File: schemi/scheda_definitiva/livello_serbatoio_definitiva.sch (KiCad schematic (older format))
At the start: 35 parts, among them J1 USB_B, J2 CONN_US, J3 CONN_LCD, SW1 SW_RST, SW2 SW_LCDON, U1 FT232RL, U2 ATmega328P-PU, Y1 16MHz

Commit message: fix a schema definitivo e assegnate footprint
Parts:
- removed D5: LED_LL, symbol Device:LED
- removed SW2: SW_LCDON, symbol Switch:SW_Push
- added J4: BTN_LED_GROUP, Connector_Molex:Molex_Micro-Latch_53254-0470_1x04_P2.00mm_Horizontal, symbol Connector:Conn_01x04_Male
- C1, C2, C3, C4, C5, C6, C7, C8: footprint (none) -> Capacitor_THT:C_Axial_L3.8mm_D2.6mm_P7.50mm_Horizontal
- D1, D2, D4: footprint (none) -> LED_THT:LED_D3.0mm
- D3: footprint (none) -> Diode_THT:D_DO-35_SOD27_P7.62mm_Horizontal
- F1: footprint (none) -> Fuse:Fuse_Littelfuse-LVR100
- J1: footprint (none) -> Connector_USB:USB_B_OST_USB-B1HSxx_Horizontal
- J2: footprint (none) -> Connector_PinHeader_1.00mm:PinHeader_1x04_P1.00mm_Vertical
- J3: footprint (none) -> Connector_PinHeader_1.00mm:PinHeader_1x16_P1.00mm_Vertical
- L1: footprint (none) -> Inductor_THT:L_Axial_L6.6mm_D2.7mm_P10.16mm_Horizontal_Vishay_IM-2
- R1, R2: value 22R -> 1k; footprint (none) -> Resistor_THT:R_Axial_DIN0207_L6.3mm_D2.5mm_P7.62mm_Horizontal
- R10, R11, R3, R4, R5, R6, R7, R8, R9: footprint (none) -> Resistor_THT:R_Axial_DIN0207_L6.3mm_D2.5mm_P7.62mm_Horizontal
- RV1: footprint (none) -> Potentiometer_THT:Potentiometer_Vishay_T73YP_Vertical
- SW1: footprint (none) -> Button_Switch_THT:SW_PUSH_6mm
- Y1: footprint (none) -> simboli_custom:Crystal_TH_AS16_5mm
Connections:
- net labels added: RX, TX
- wire segments 159 -> 154
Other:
- moved on the sheet: D4, J3, R10, R11, R8, R9, RV1

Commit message: caricamento prima bozza PCB + piccoli fix a footprint
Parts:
- J2: footprint Connector_PinHeader_1.00mm:PinHeader_1x04_P1.00mm_Vertical -> Connector_Molex:Molex_Micro-Latch_53254-0470_1x04_P2.00mm_Horizontal
- J3: footprint Connector_PinHeader_1.00mm:PinHeader_1x16_P1.00mm_Vertical -> Connector_PinHeader_1.27mm:PinHeader_1x16_P1.27mm_Vertical
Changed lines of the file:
@@
 F 0 "J2" H 10500 1050 50  0000 C CNN
 F 1 "CONN_US" H 10750 1300 50  0000 C CNN
-F 2 "Connector_PinHeader_1.00mm:PinHeader_1x04_P1.00mm_Vertical" H 10500 1350 50  0001 C CNN
+F 2 "Connector_Molex:Molex_Micro-Latch_53254-0470_1x04_P2.00mm_Horizontal" H 10500 1350 50  0001 C CNN
 F 3 "~" H 10500 1350 50  0001 C CNN
 	1    10500 1350
@@
 F 0 "J3" H 10492 3125 50  0000 C CNN
 F 1 "CONN_LCD" H 10492 3216 50  0000 C CNN
-F 2 "Connector_PinHeader_1.00mm:PinHeader_1x16_P1.00mm_Vertical" H 10600 4150 50  0001 C CNN
+F 2 "Connector_PinHeader_1.27mm:PinHeader_1x16_P1.27mm_Vertical" H 10600 4150 50  0001 C CNN
 F 3 "~" H 10600 4150 50  0001 C CNN
 	1    10600 4150

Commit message: modifiche a scheda definitiva - aggiunto footprint LCD di riferimento - modificato schematico per aggiungere connettore ICSP e fori di montaggio a massa - ricollocati connettori - da rivedere collocazione MCU per conflitto con LCD
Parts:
- removed R10: 390, Resistor_THT:R_Axial_DIN0207_L6.3mm_D2.5mm_P7.62mm_Horizontal, symbol Device:R
- added H1: HOLE1, MountingHole:MountingHole_3mm_Pad_Via, symbol Mechanical:MountingHole_Pad
- added H2: HOLE2, MountingHole:MountingHole_3mm_Pad_Via, symbol Mechanical:MountingHole_Pad
- added H3: HOLE3, MountingHole:MountingHole_3mm_Pad_Via, symbol Mechanical:MountingHole_Pad
- added H4: HOLE4, MountingHole:MountingHole_3mm_Pad_Via, symbol Mechanical:MountingHole_Pad
- added J5: Conn_01x06_Male, Connector_PinHeader_2.54mm:PinHeader_1x06_P2.54mm_Horizontal, symbol Connector:Conn_01x06_Male
- J3: footprint Connector_PinHeader_1.27mm:PinHeader_1x16_P1.27mm_Vertical -> Connector_PinSocket_2.54mm:PinSocket_1x16_P2.54mm_Vertical
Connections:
- net labels added: ICSP_MISO, ICSP_MOSI, ICSP_RST, ICSP_SCK
- wire segments 154 -> 179
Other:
- note added: "ICSP - Bootloader"
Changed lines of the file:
@@
 Text GLabel 6800 2450 2    50   Output ~ 0
 D11
-Wire Wire Line
-	6650 2450 6800 2450
-Wire Wire Line
-	6650 2550 6800 2550
 Text GLabel 6800 2550 2    50   Input ~ 0
 D12
@@
 D13
 Wire Wire Line
-	6650 2650 6800 2650
+	6650 2650 6750 2650
 $Comp
 L power:GND #PWR06
@@
 Wire Notes Line
 	10850 2600 10850 6300
-Text GLabel 9500 4400 2    50   Output ~ 0
+Text GLabel 9100 4400 2    50   Output ~ 0
 BLA
-$Comp
-L Device:R R10
-U 1 1 5F131632
-P 9150 4400
-F 0 "R10" V 9050 4400 50  0000 C CNN
-F 1 "390" V 9150 4400 50  0000 C CNN
-F 2 "Resistor_THT:R_Axial_DIN0207_L6.3mm_D2.5mm_P7.62mm_Horizontal" V 9080 4400 50  0001 C CNN
-F 3 "~" H 9150 4400 50  0001 C CNN
-	1    9150 4400
-	0    1    1    0
-$EndComp
-Text GLabel 8800 4400 0    50   Input ~ 0
+Text GLabel 8850 4400 0    50   Input ~ 0
 D9
-Wire Wire Line
-	8800 4400 9000 4400
-Wire Wire Line
-	9300 4400 9500 4400
 $Comp
 L power:VCC #PWR018
@@
 F 0 "J3" H 10492 3125 50  0000 C CNN
 F 1 "CONN_LCD" H 10492 3216 50  0000 C CNN
-F 2 "Connector_PinHeader_1.27mm:PinHeader_1x16_P1.27mm_Vertical" H 10600 4150 50  0001 C CNN
+F 2 "Connector_PinSocket_2.54mm:PinSocket_1x16_P2.54mm_Vertical" H 10600 4150 50  0001 C CNN
 F 3 "~" H 10600 4150 50  0001 C CNN
 	1    10600 4150
@@
 Wire Wire Line
 	8100 1600 8100 1850
+Wire Wire Line
+	8850 4400 9100 4400
+Wire Notes Line
+	5400 5350 8050 5350
+Wire Notes Line
+	8050 5350 8050 6450
+Wire Notes Line
+	8050 6450 5400 6450
+Wire Notes Line
+	5400 6450 5400 5350
+Text Notes 6350 5450 0    50   ~ 0
+ICSP - Bootloader
+$Comp
+L Connector:Conn_01x06_Male J5
+U 1 1 5F49926C
+P 7150 5900
+F 0 "J5" H 7122 5782 50  0000 R CNN
+F 1 "Conn_01x06_Male" H 7550 6200 50  0000 R CNN
+F 2 "Connector_PinHeader_2.54mm:PinHeader_1x06_P2.54mm_Horizontal" H 7150 5900 50  0001 C CNN
+F 3 "~" H 7150 5900 50  0001 C CNN
+	1    7150 5900
+	-1   0    0    1
+$EndComp
+Text GLabel 6550 6100 0    50   Input ~ 0
+ICSP_MISO
+Text GLabel 6550 5800 0    50   Input ~ 0
+ICSP_MOSI
+$Comp
+L power:VCC #PWR017
+U 1 1 5F4B97E7
+P 6550 6000
+F 0 "#PWR017" H 6550 5850 50  0001 C CNN
+F 1 "VCC" V 6565 6127 50  0000 L CNN
+F 2 "" H 6550 6000 50  0001 C CNN
+F 3 "" H 6550 6000 50  0001 C CNN
+	1    6550 6000
+	0    -1   -1   0
+$EndComp
+Text GLabel 6550 5900 0    50   Input ~ 0
+ICSP_SCK
+Text GLabel 6550 5700 0    50   Input ~ 0
+ICSP_RST
+$Comp
+L power:GND #PWR07
+U 1 1 5F4BAD5C
+P 6550 5600
+F 0 "#PWR07" H 6550 5350 50  0001 C CNN
+F 1 "GND" V 6555 5472 50  0000 R CNN
+F 2 "" H 6550 5600 50  0001 C CNN
+F 3 "" H 6550 5600 50  0001 C CNN
+	1    6550 5600
+	0    1    1    0
+$EndComp
+Wire Wire Line
+	6550 5600 6950 5600
+Wire Wire Line
+	6550 5700 6950 5700
+Wire Wire Line
+	6550 5800 6950 5800
+Wire Wire Line
+	6550 5900 6950 5900
+Wire Wire Line
+	6550 6000 6950 6000
+Wire Wire Line
+	6550 6100 6950 6100
+Text GLabel 7100 2350 2    50   Output ~ 0
+ICSP_MISO
+Text GLabel 7100 2250 2    50   Output ~ 0
+ICSP_MOSI
+Text GLabel 7100 2450 2    50   Output ~ 0
+ICSP_SCK
+Wire Wire Line
+	7000 2450 7000 2700
+Wire Wire Line
+	7000 2700 6750 2700
+Wire Wire Line
+	6750 2700 6750 2650
+Wire Wire Line
+	7000 2450 7100 2450
+Connection ~ 6750 2650
+Wire Wire Line
+	6750 2650 6800 2650
+Wire Wire Line
+	6650 2450 6700 2450
+Wire Wire Line
+	6650 2550 6750 2550
+Wire Wire Line
+	7100 2350 6750 2350
+Wire Wire Line
+	6750 2350 6750 2550
+Connection ~ 6750 2550
+Wire Wire Line
+	6750 2550 6800 2550
+Wire Wire Line
+	7100 2250 7050 2250
+Wire Wire Line
+	7050 2250 7050 2300
+Wire Wire Line
+	7050 2300 6700 2300
+Wire Wire Line
+	6700 2300 6700 2450
+Connection ~ 6700 2450
+Wire Wire Line
+	6700 2450 6800 2450
+Text GLabel 3600 5950 3    50   Output ~ 0
+ICSP_RST
+Wire Wire Line
+	3600 5700 3600 5950
+$Comp
+L Mechanical:MountingHole_Pad H1
+U 1 1 5F5C5141
+P 2500 1000
+F 0 "H1" H 2600 1049 50  0000 L CNN
+F 1 "HOLE1" H 2400 1200 50  0000 L CNN
+F 2 "MountingHole:MountingHole_3mm_Pad_Via" H 2500 1000 50  0001 C CNN
+F 3 "~" H 2500 1000 50  0001 C CNN
+	1    2500 1000
+	1    0    0    -1
+$EndComp
+$Comp
+L Mechanical:MountingHole_Pad H2
+U 1 1 5F5C614B
+P 2850 1000
+F 0 "H2" H 2950 1049 50  0000 L CNN
+F 1 "HOLE2" H 2800 1200 50  0000 L CNN
+F 2 "MountingHole:MountingHole_3mm_Pad_Via" H 2850 1000 50  0001 C CNN
+F 3 "~" H 2850 1000 50  0001 C CNN
+	1    2850 1000
+	1    0    0    -1
+$EndComp
+$Comp
+L Mechanical:MountingHole_Pad H3
+U 1 1 5F5C6841
+P 3200 1000
+F 0 "H3" H 3300 1049 50  0000 L CNN
+F 1 "HOLE3" H 3100 1200 50  0000 L CNN
+F 2 "MountingHole:MountingHole_3mm_Pad_Via" H 3200 1000 50  0001 C CNN
+F 3 "~" H 3200 1000 50  0001 C CNN
+	1    3200 1000
+	1    0    0    -1
+$EndComp
+$Comp
+L Mechanical:MountingHole_Pad H4
+U 1 1 5F5C77FA
+P 3550 1000
+F 0 "H4" H 3650 1049 50  0000 L CNN
+F 1 "HOLE4" H 3450 1200 50  0000 L CNN
+F 2 "MountingHole:MountingHole_3mm_Pad_Via" H 3550 1000 50  0001 C CNN
+F 3 "~" H 3550 1000 50  0001 C CNN
+	1    3550 1000
+	1    0    0    -1
+$EndComp
+$Comp
+L power:GND #PWR022
+U 1 1 5F5C8BD6
+P 3050 1300
+F 0 "#PWR022" H 3050 1050 50  0001 C CNN
+F 1 "GND" H 3055 1127 50  0000 C CNN
+F 2 "" H 3050 1300 50  0001 C CNN
+F 3 "" H 3050 1300 50  0001 C CNN
+	1    3050 1300
+	1    0    0    -1
+$EndComp
+Wire Wire Line
+	2500 1100 2850 1100
+Wire Wire Line
+	2850 1100 3200 1100
+Connection ~ 2850 1100
+Wire Wire Line
+	3200 1100 3550 1100
+Connection ~ 3200 1100
+Wire Wire Line
+	3200 1100 3200 1150
+Wire Wire Line
+	3200 1150 3050 1150
+Wire Wire Line
+	3050 1150 3050 1300
 $EndSCHEMATC

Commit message: riposizionati connettori + auto-routing eseguito con freerouting
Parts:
- removed C5: 100nF, Capacitor_THT:C_Axial_L3.8mm_D2.6mm_P7.50mm_Horizontal, symbol Device:C
- removed L1: 10uH, Inductor_THT:L_Axial_L6.6mm_D2.7mm_P10.16mm_Horizontal_Vishay_IM-2, symbol Device:L
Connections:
- wire segments 179 -> 173
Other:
- moved on the sheet: C6
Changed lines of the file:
@@
 $EndDescr
-$Comp
-L MCU_Microchip_ATmega:ATmega328P-PU U2
-U 1 1 5F0B08F0
-P 6050 3350
-F 0 "U2" H 5650 4800 50  0000 R CNN
-F 1 "ATmega328P-PU" H 6250 3600 50  0000 R CNN
-F 2 "Package_DIP:DIP-28_W7.62mm" H 6050 3350 50  0001 C CIN
-F 3 "http://ww1.microchip.com/downloads/en/DeviceDoc/ATmega328_P%20AVR%20MCU%20with%20picoPower%20Technology%20Data%20Sheet%2040001984A.pdf" H 6050 3350 50  0001 C CNN
-	1    6050 3350
-	1    0    0    -1
-$EndComp
 $Comp
 L Interface_USB:FT232RL U1
@@
 Connection ~ 7500 2650
 $Comp
-L Device:C C5
-U 1 1 5F1D4DDB
-P 6550 1350
-F 0 "C5" V 6298 1350 50  0000 C CNN
-F 1 "100nF" V 6389 1350 50  0000 C CNN
-F 2 "Capacitor_THT:C_Axial_L3.8mm_D2.6mm_P7.50mm_Horizontal" H 6588 1200 50  0001 C CNN
-F 3 "~" H 6550 1350 50  0001 C CNN
-	1    6550 1350
-	0    1    1    0
-$EndComp
-$Comp
 L power:GND #PWR08
 U 1 1 5F1D54A8
-P 6900 1650
-F 0 "#PWR08" H 6900 1400 50  0001 C CNN
-F 1 "GND" V 6905 1522 50  0000 R CNN
-F 2 "" H 6900 1650 50  0001 C CNN
-F 3 "" H 6900 1650 50  0001 C CNN
-	1    6900 1650
+P 6700 1700
+F 0 "#PWR08" H 6700 1450 50  0001 C CNN
+F 1 "GND" V 6705 1572 50  0000 R CNN
+F 2 "" H 6700 1700 50  0001 C CNN
+F 3 "" H 6700 1700 50  0001 C CNN
+	1    6700 1700
 	0    -1   -1   0
 $EndComp
@@
 L Device:C C6
 U 1 1 5F0BF95B
-P 6550 1750
-F 0 "C6" V 6298 1750 50  0000 C CNN
-F 1 "100nF" V 6389 1750 50  0000 C CNN
-F 2 "Capacitor_THT:C_Axial_L3.8mm_D2.6mm_P7.50mm_Horizontal" H 6588 1600 50  0001 C CNN
-F 3 "~" H 6550 1750 50  0001 C CNN
-	1    6550 1750
-	0    1    1    0
-$EndComp
-$Comp
-L Device:L L1
-U 1 1 5F0F5110
-P 6150 1600
-F 0 "L1" H 6203 1646 50  0000 L CNN
-F 1 "10uH" H 6203 1555 50  0000 L CNN
-F 2 "Inductor_THT:L_Axial_L6.6mm_D2.7mm_P10.16mm_Horizontal_Vishay_IM-2" H 6150 1600 50  0001 C CNN
-F 3 "~" H 6150 1600 50  0001 C CNN
-	1    6150 1600
-	1    0    0    -1
-$EndComp
-Wire Wire Line
-	6400 1350 6050 1350
-Wire Wire Line
-	6150 1450 6150 950
-Wire Wire Line
-	6050 1350 6050 950
-Wire Wire Line
-	6150 1750 6400 1750
-Wire Wire Line
-	6700 1350 6900 1350
-Wire Wire Line
-	6900 1350 6900 1650
-Wire Wire Line
-	6900 1650 6900 1750
-Wire Wire Line
-	6900 1750 6700 1750
-Connection ~ 6900 1650
+P 6450 1700
+F 0 "C6" V 6700 1700 50  0000 C CNN
+F 1 "100nF" V 6600 1700 50  0000 C CNN
+F 2 "Capacitor_THT:C_Axial_L3.8mm_D2.6mm_P7.50mm_Horizontal" H 6488 1550 50  0001 C CNN
+F 3 "~" H 6450 1700 50  0001 C CNN
+	1    6450 1700
+	0    -1   -1   0
+$EndComp
 $Comp
 L power:GND #PWR02
@@
 NoConn ~ 3850 3950
 NoConn ~ 3850 4050
-Wire Wire Line
-	6050 1350 6050 1850
-Connection ~ 6050 1350
 Text GLabel 6800 4050 2    50   Input ~ 0
 D2
@@
 Connection ~ 3150 2350
 Connection ~ 2950 2350
-Wire Wire Line
-	6150 1850 6150 1750
-Connection ~ 6150 1750
 Wire Wire Line
 	2150 2350 2950 2350
@@
 Connection ~ 2150 2150
 $Comp
-L power:PWR_FLAG #FLG01
-U 1 1 5F582FA7
-P 6250 1850
-F 0 "#FLG01" H 6250 1925 50  0001 C CNN
-F 1 "PWR_FLAG" V 6250 1978 50  0000 L CNN
-F 2 "" H 6250 1850 50  0001 C CNN
-F 3 "~" H 6250 1850 50  0001 C CNN
-	1    6250 1850
-	0    1    1    0
-$EndComp
-Wire Wire Line
-	6150 950  6100 950
-$Comp
 L power:VCC #PWR0101
 U 1 1 5F5AA697
-P 6100 950
-F 0 "#PWR0101" H 6100 800 50  0001 C CNN
-F 1 "VCC" H 6115 1123 50  0000 C CNN
-F 2 "" H 6100 950 50  0001 C CNN
-F 3 "" H 6100 950 50  0001 C CNN
-	1    6100 950
-	1    0    0    -1
-$EndComp
-Connection ~ 6100 950
-Wire Wire Line
-	6100 950  6050 950
-Wire Wire Line
-	6250 1850 6150 1850
-Connection ~ 6150 1850
+P 6100 1500
+F 0 "#PWR0101" H 6100 1350 50  0001 C CNN
+F 1 "VCC" H 6115 1673 50  0000 C CNN
+F 2 "" H 6100 1500 50  0001 C CNN
+F 3 "" H 6100 1500 50  0001 C CNN
+	1    6100 1500
+	1    0    0    -1
+$EndComp
 Text Notes 9800 900  0    50   ~ 0
 Ultrasonic sensor
@@
 	-1   0    0    1
 $EndComp
+Text GLabel 6550 5900 0    50   Input ~ 0
+ICSP_MISO
 Text GLabel 6550 6100 0    50   Input ~ 0
-ICSP_MISO
-Text GLabel 6550 5800 0    50   Input ~ 0
 ICSP_MOSI
 $Comp
@@
 	0    -1   -1   0
 $EndComp
-Text GLabel 6550 5900 0    50   Input ~ 0
+Text GLabel 6550 5800 0    50   Input ~ 0
 ICSP_SCK
 Text GLabel 6550 5700 0    50   Input ~ 0
@@
 Wire Wire Line
 	3050 1150 3050 1300
+$Comp
+L MCU_Microchip_ATmega:ATmega328P-PU U2
+U 1 1 5F0B08F0
+P 6050 3350
+F 0 "U2" H 5650 4800 50  0000 R CNN
+F 1 "ATmega328P-PU" H 6250 3600 50  0000 R CNN
+F 2 "Package_DIP:DIP-28_W7.62mm" H 6050 3350 50  0001 C CIN
+F 3 "http://ww1.microchip.com/downloads/en/DeviceDoc/ATmega328_P%20AVR%20MCU%20with%20picoPower%20Technology%20Data%20Sheet%2040001984A.pdf" H 6050 3350 50  0001 C CNN
+	1    6050 3350
+	1    0    0    -1
+$EndComp
+Wire Wire Line
+	6100 1500 6100 1700
+Wire Wire Line
+	6100 1700 6050 1700
+Wire Wire Line
+	6050 1700 6050 1850
+Wire Wire Line
+	6100 1700 6150 1700
+Wire Wire Line
+	6150 1700 6150 1850
+Connection ~ 6100 1700
+Connection ~ 6150 1700
+Wire Wire Line
+	6150 1700 6300 1700
+Wire Wire Line
+	6700 1700 6600 1700
 $EndSCHEMATC

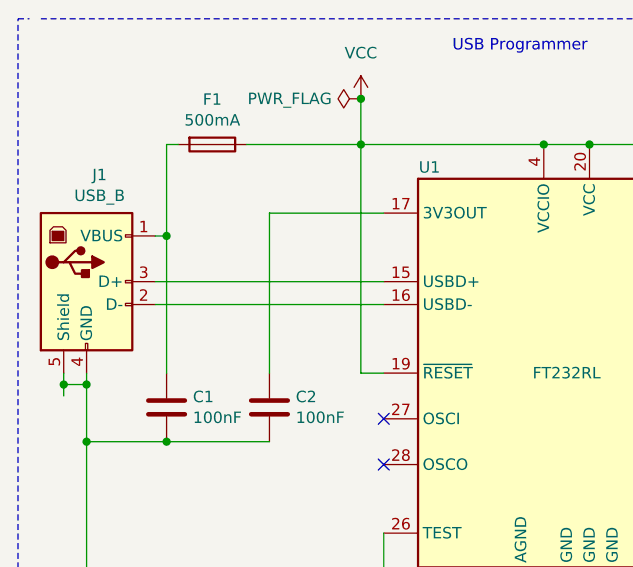
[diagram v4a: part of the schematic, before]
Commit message: fix alimentazioni + introduzione coppia differenziale per USB - da rivedere piste USB per match lunghezza/skew/impedenza
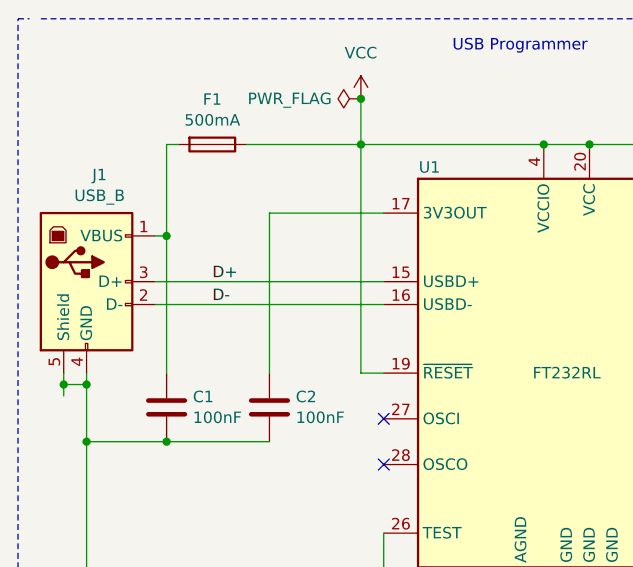
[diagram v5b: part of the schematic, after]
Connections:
- net D+: now reaches J1.3 (D+), U1.15 (USBD+)
- net D-: now reaches J1.2 (D-), U1.16 (USBD-)
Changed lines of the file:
@@
 Wire Wire Line
 	6700 1700 6600 1700
+Text Label 1500 2950 0    50   ~ 0
+D+
+Text Label 1500 3050 0    50   ~ 0
+D-
 $EndSCHEMATC
